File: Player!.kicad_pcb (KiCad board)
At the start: 2 copper layers, 95.2 x 38.1 mm, 25 parts, among them J1 USB4085-GF-A_REVA4, SW1 SW_Push, SW2 SW_Push, SW3 SW_Push, SW4 SW_Push, SW5 RotaryEncoder_Switch

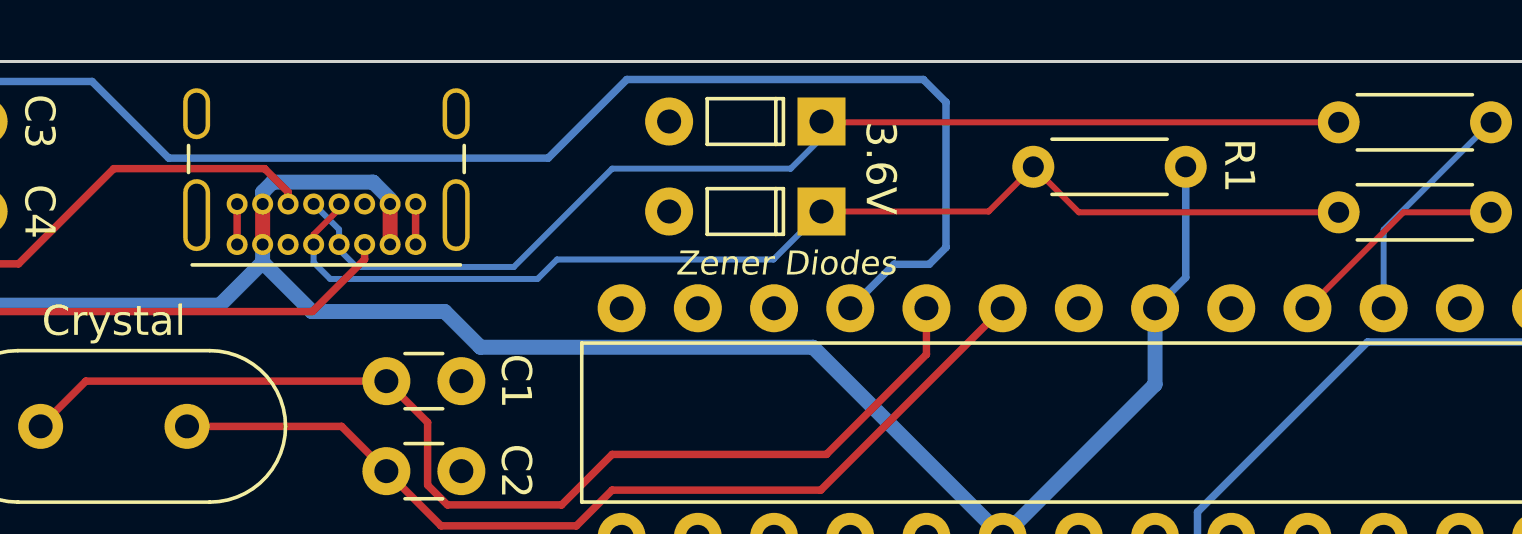
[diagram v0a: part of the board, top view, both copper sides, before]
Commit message: Updated Models
Changed type C footprint & model, updated to use .step models in 3d for all components
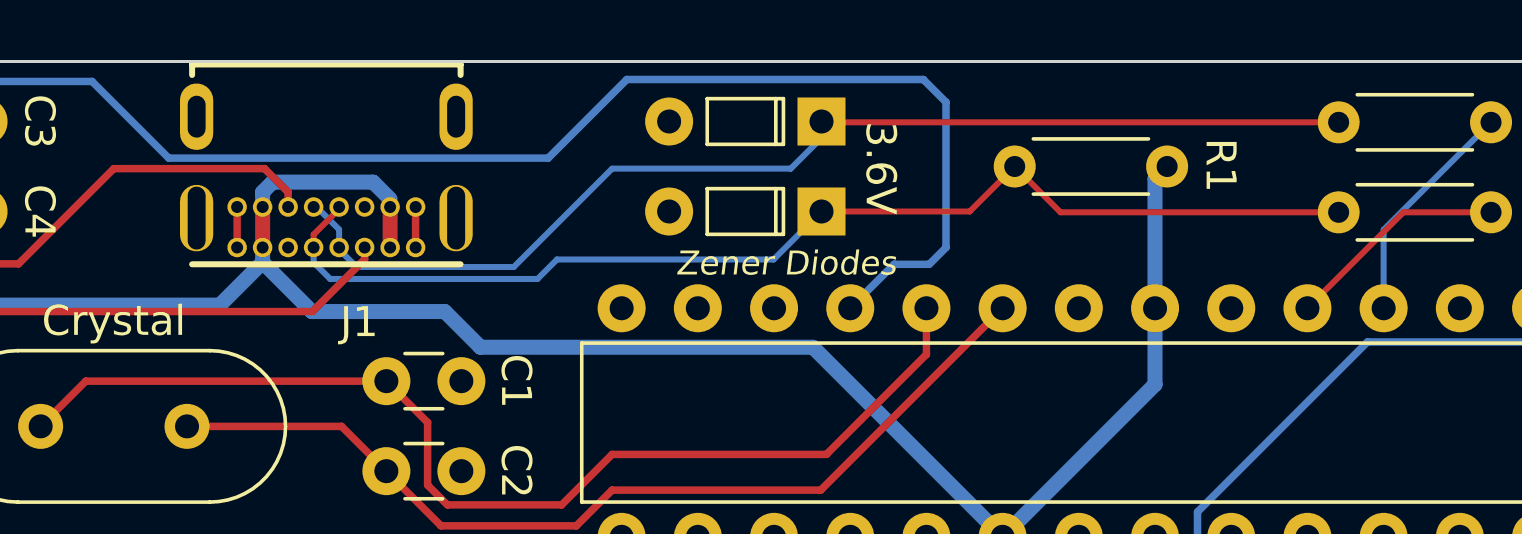
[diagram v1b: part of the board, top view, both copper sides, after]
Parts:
- J1: footprint Keyboard Stuff:USB_C_Receptacle_GCT_USB4085 -> Keyboard Stuff:GCT_USB4085-GF-A_REVA4
- moved J1 4.93 mm to (47.6, 2.17)
- moved R1 0.62 mm to (75.7, 3.50)

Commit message: Updating PCB and Models for Case
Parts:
- moved C1 12.8 mm to (59.0, 2.02)
- moved C2 12.8 mm to (59.0, 5.02)
- moved Crystal1 7.07 mm to (45.2, 12.2)
- moved DN1 6.42 mm to (70.5, 2.02)
- moved DP1 6.42 mm to (70.5, 5.02)
- moved R2 4.72 mm to (34.2, 10.7)
- moved R4 4.72 mm to (34.2, 13.7)
- moved R1 4.72 mm to (23.1, 10.7)
- moved R3 4.72 mm to (23.1, 13.7)
- moved R5 4.17 mm to (79.8, 3.52)
- moved Power 2.59 mm to (16.4, 2.25), turned to -90 degrees
- moved Reset 2.50 mm to (4.00, 11.3)
- moved R6 2.45 mm to (83.8, 2.02)
- moved R7 2.45 mm to (83.8, 5.02)
- moved Boot 1.97 mm to (4.00, 2.25)
- renumbered ATMega328 to ATmega328, R7 to R1, R4 to R3, R3 to R4, R1 to R5, R5 to R7
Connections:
- J1 pad P1: (no net) -> GND
- J1 pad P2: (no net) -> GND
- J1 pad P3: (no net) -> GND
- J1 pad P4: (no net) -> GND
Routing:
- net /BOOT: track 78.3 -> 64.7 mm
- net /XTAL2: track 36.7 -> 29.2 mm
- net /XTAL1: track 31.6 -> 26.2 mm
- net /CC1: track 23.0 -> 17.8 mm
- net /LED: track 6.90 -> 12.0 mm
- net D+: track 7.68 -> 12.6 mm
- net /CC2: track 20.6 -> 15.9 mm
- net /RST: track 95.2 -> 90.6 mm
- net /DN: track 38.8 -> 41.6 mm
- net /DP: track 37.7 -> 40.3 mm
- net D-: track 7.44 -> 9.55 mm
- net +5V: track 99.2 -> 97.4 mm
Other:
- outline, holes or cut-outs redrawn
- board text added: "Player! (V1.2) by Johnboysmooth"
- board text removed: "Player! (V1.1) by Johnboysmooth"
